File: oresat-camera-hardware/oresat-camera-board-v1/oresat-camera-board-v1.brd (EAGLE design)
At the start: 31.5 x 14 mm, 41 parts, among them J1 4-1734742-0, U1 AR0134CSSM00SPCA0, U2 TPS70618DRVR, U3 TPS71928-28DRVT, U4 TPS71928-28DRVT, X1 KC2520B27.0000C10E00

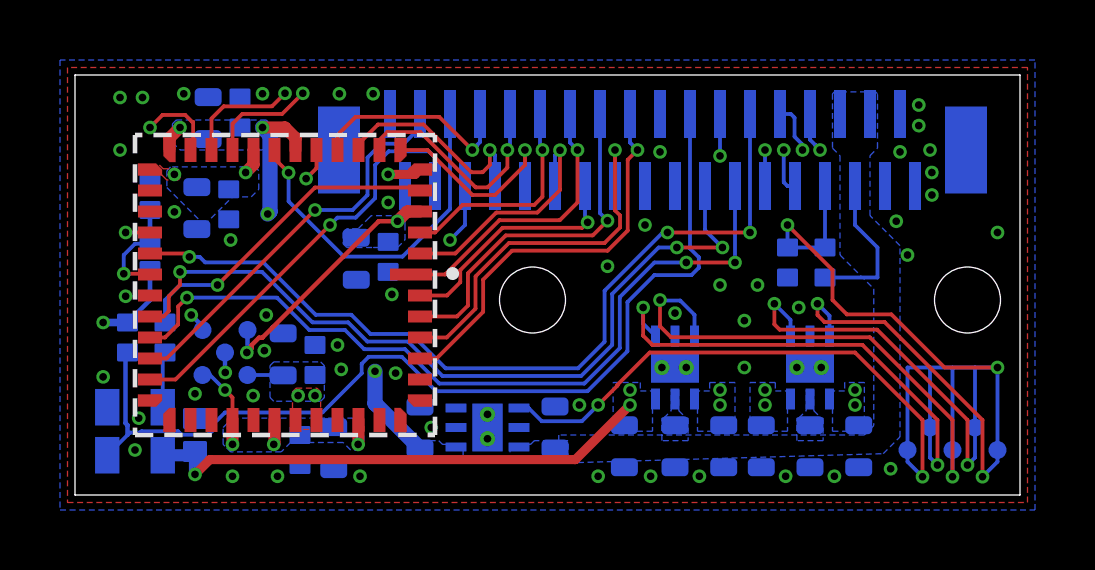
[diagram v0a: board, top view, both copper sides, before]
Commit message: rerouted camera bus
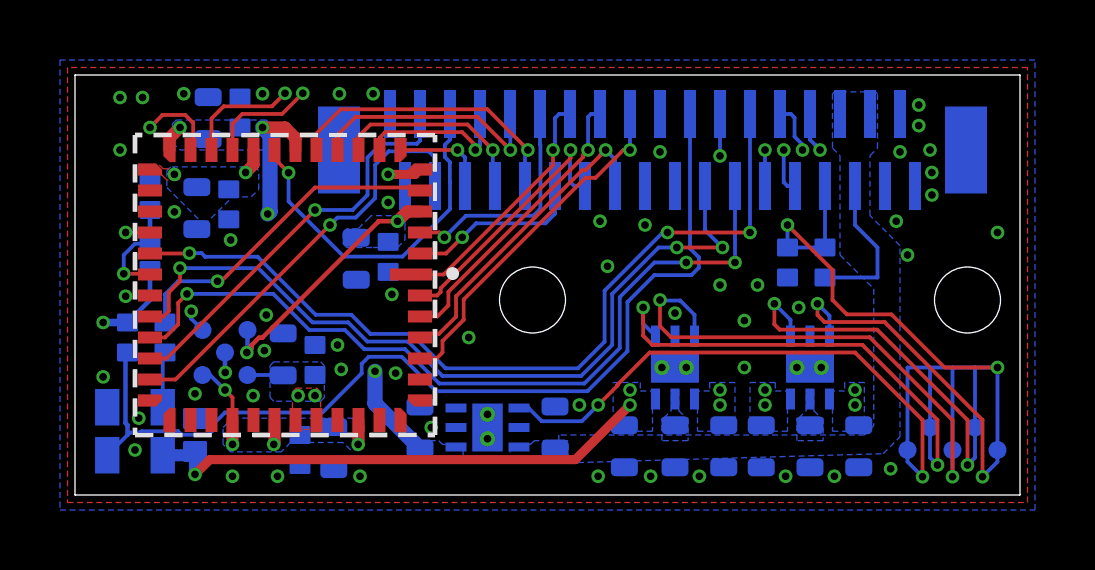
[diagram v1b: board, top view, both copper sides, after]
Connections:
- net D10: now also J1.28; no longer J1.30
- net D11: now also J1.27; no longer J1.31
- net D7: now also J1.31; no longer J1.27
- net D8: now also J1.30; no longer J1.28
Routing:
- net D7: track 6.89 -> 3.20 mm
- net D8: track 7.57 -> 5.28 mm
- net D1: track 12.7 -> 10.5 mm
- net D5: track 8.13 -> 5.97 mm
- net D2: track 11.9 -> 9.75 mm
- net D0: track 13.4 -> 11.7 mm
- net D4: track 9.60 -> 8.39 mm
- net D10: track 7.01 -> 8.18 mm
- net D11: track 8.75 -> 9.74 mm, vias 2 -> 1
- net D3: track 8.08 -> 8.89 mm
- net D9: track 7.38 -> 6.68 mm
- net GND: vias 52 -> 54
